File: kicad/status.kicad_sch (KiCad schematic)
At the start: 48 parts, among them J1 Bus_PCI_Express_x1, J2 PPTC041LGBN-RC, J3 Conn_01x04, J5 TF-115-BCP9, J6 USB_C_Receptacle_USB2.0_16P, J7 Conn_01x02, U1 MCP25625T-E/ML, U2 RP2040, U4 W25Q128JVP, X1 ABM8-272-T3, Y1 X322516MLB4SI

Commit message: Update PCB Layout and Change file Names to Status
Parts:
- removed J5: TF-115-BCP9, TF115BCP9, symbol TF-115-BCP9:TF-115-BCP9
- added J4: 503398-1892, 503398-1892:MOLEX_503398-1892, symbol MicroSD:503398-1892
- added R15: 10K, Resistor_SMD:R_0402_1005Metric, symbol Device:R
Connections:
- net +3.3V: now also J2.3, S11.C, J4.4 (VDD); no longer J2.2
- net CS_SD: now also J4.2 (CD/DAT3^2)
- net GND: now also J2.4, J4.6 (VSS), J4.9 (VSS__1), J4.P1 (SHIELD), J4.P2 (SHIELD__1), J4.P3 (SHIELD__2), J4.P4 (SHIELD__3), R15.2; no longer J2.1, S11.A
- net MISO: now also J4.7 (DAT0)
- net MOSI: now also J4.3 (CMD)
- net SCK: now also J4.5 (CLK)
- net SCL: now also J2.2; no longer J2.3
- net SDA: now also J2.1; no longer J2.4
- net RUN: now reaches U2.26 (RUN)
- net RUN: now also S11.A, R15.1; no longer S11.C
- removed net +BAT: J1.A16 (PERp0), J1.A17 (PERn0), J1.A18 (GND), J1.B16 (GND), J1.B17 (~{PRSNT2}), J1.B18 (GND)
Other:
- moved on the sheet: S11

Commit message: Pcb layout updated
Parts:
- removed J1: Bus_PCI_Express_x1, Connector_PCBEdge:BUS_PCIexpress_x1, symbol Connector:Bus_PCI_Express_x1
- removed U1: MCP25625T-E/ML, challenge_template:QFN28_6X6MC_MCH, symbol challenge symbols:MCP25625T-E_ML
- added J5: Bus_PCI_Express_x1, Connector_PCBEdge:BUS_PCIexpress_x1, symbol Connector:Bus_PCI_Express_x1
- added U3: MCP25625T-E/ML, QFN28_6X6MC_MCH, symbol challenge symbols:MCP25625T-E_ML
- D1: JLC Link https://jlcpcb.com/partdetail/177361-BL_HKC37A_AVTRB/C165978 -> https://jlcpcb.com/partdetail/EverlightElec-16_213_T3D_AP1Q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; LCSC Part # C165978 -> C74340
- J4: JLC Link (none) -> https://jlcpcb.com/parts/componentSearch?searchTxt=%2050339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; JLC link https://jlcpcb.com/parts/componentSearch?searchTxt=%2050339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 -> (none); LCSC Part # (none) -> C428492
- R10, R13, R15, R7, R8, R9: JLC Link https://jlcpcb.com/partdetail/Yageo-RC0402JR0710KL/C60489 -> https://jlcpcb.com/partdetail/YAGEO-RC0402FR0710KL/C60490; LCSC Part # C60489 -> C60490
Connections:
- net +3.3V: now also J5.A10 (+3.3V), J5.A11 (~{PERST}), J5.A9 (+3.3V), J5.B10 (3.3Vaux), J5.B11 (~{WAKE}), J5.B9 (JTAG1), U3.11 (VIO), U3.3 (VDD)
- net +5V: now also J5.A12 (GND), J5.A13 (REFCLK+), J5.A14 (REFCLK-), J5.B12 (RSVD), J5.B13 (GND), J5.B14 (PETp0), U3.19 (VDDA)
- net CANH: now also J5.A1 (~{PRSNT1}), U3.13 (CANH)
- net CANL: now also J5.A3 (+12V), U3.12 (CANL)
- net CS: now also U3.1 (*CS)
- net GND: now also J5.A4 (GND), J5.A5 (JTAG2), J5.A6 (JTAG3), J5.A7 (JTAG4), J5.B1 (+12V), J5.B2 (+12V), J5.B3 (+12V), J5.B4 (GND), J5.B5 (SMCLK), J5.B6 (SMDAT), J5.B7 (GND), U3.18 (VSS), U3.22 (GND), U3.29 (EPAD)
- net INT: now also U3.25 (*INT)
- net MISO: now also U3.28 (SO)
- net MOSI: now also U3.27 (SI)
- net OSC1: now also U3.21 (OSC1)
- net OSC2: now also U3.20 (OSC2)
- net RESET: now also U3.2 (*RESET)
- net RX: now also U3.10 (RXD), U3.5 (RXCAN)
- net SCK: now also U3.26 (SCK)
- net STBY: now also U3.15 (STBY)
- net TX: now also U3.16 (TXD), U3.4 (TXCAN)
- no-connect marks 17 -> 39

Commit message: SD Card Update
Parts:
- added R16, R17, R18, R19: 10K, Resistor_SMD:R_0402_1005Metric, symbol Device:R
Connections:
- net +3.3V: now also R16.1, R17.1, R18.1, R19.1
- net MISO: now also R17.2
- net MOSI: now also R16.2
- net at J4.1 (DAT2): now also R19.2
- net at J4.8 (DAT1): now also R18.2
- no-connect marks 39 -> 37

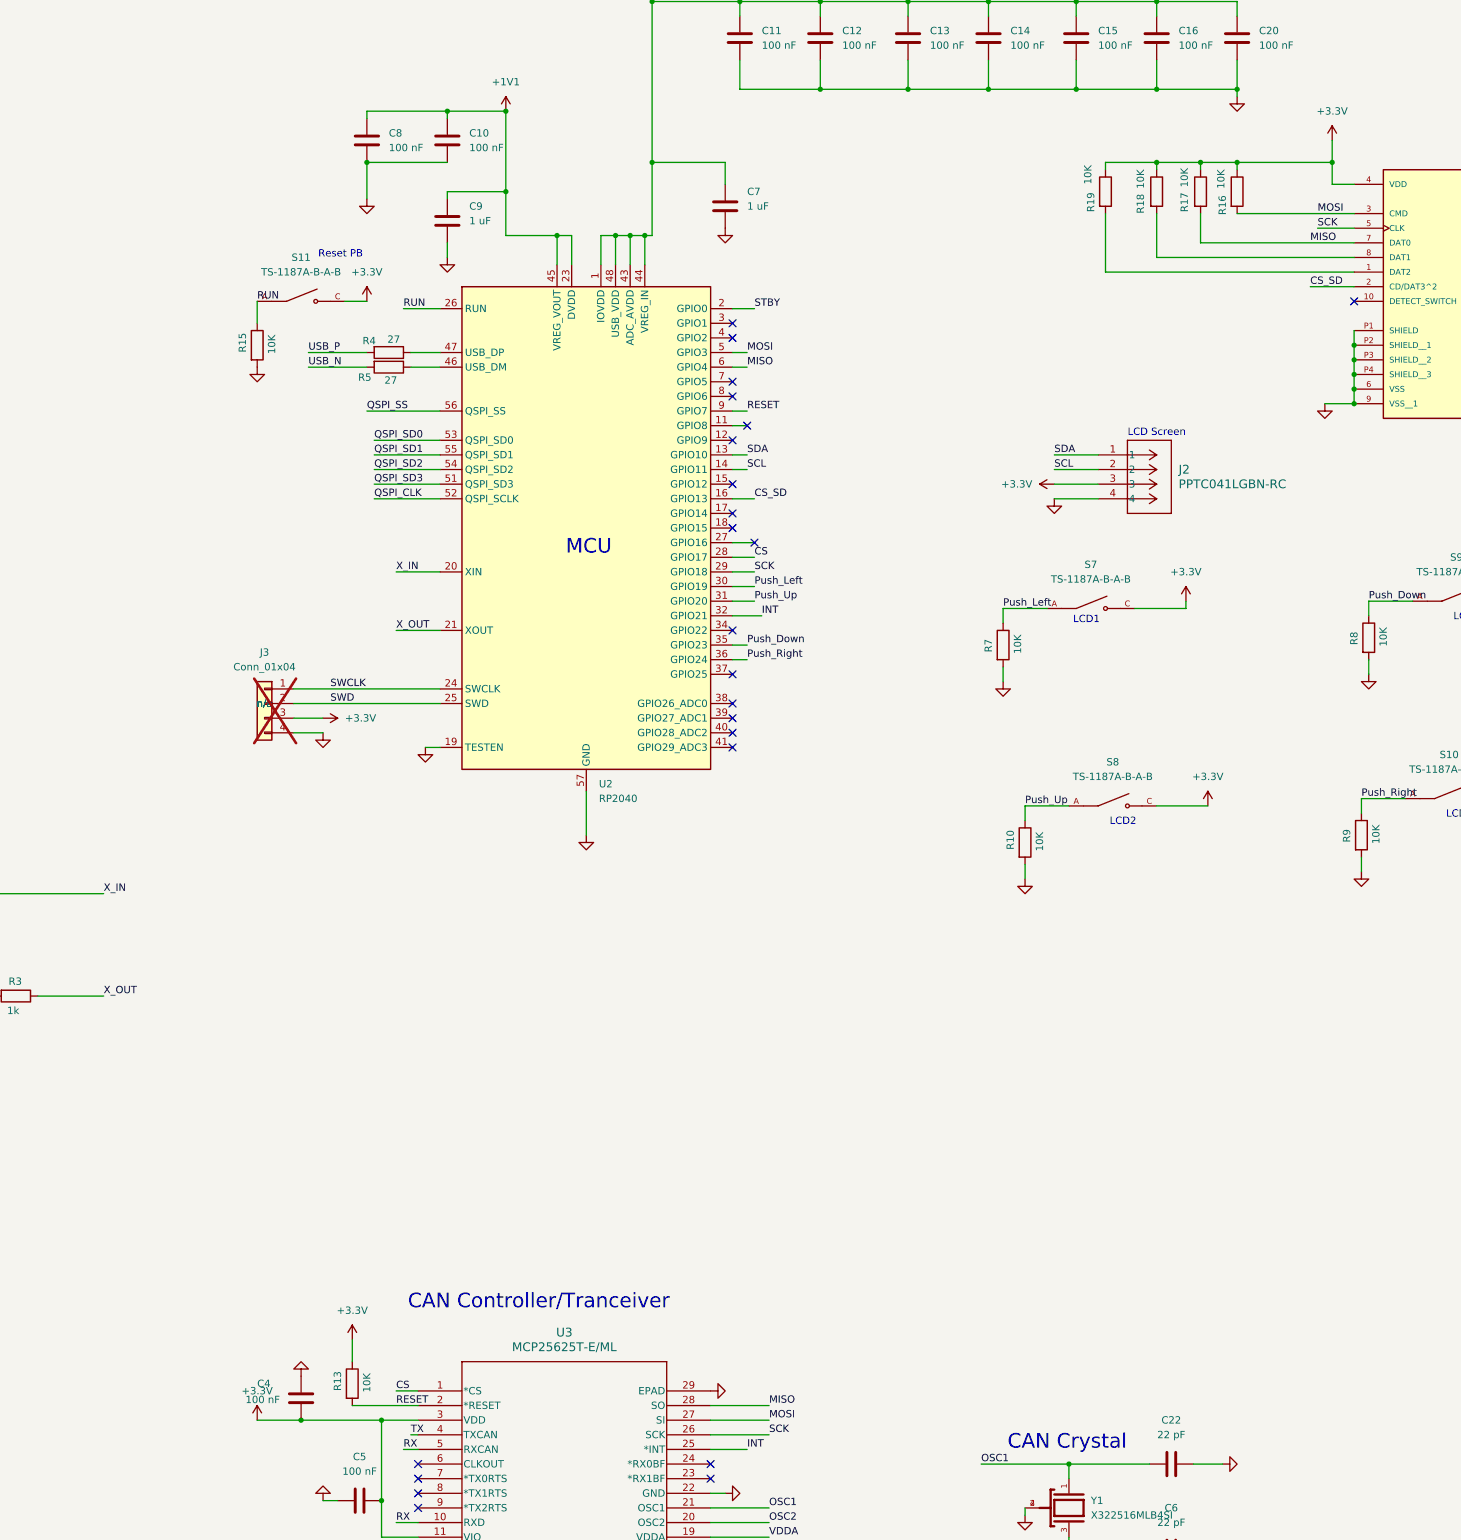
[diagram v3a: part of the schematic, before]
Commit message: General Updates
Moved CAN transmitter to separate SPI line.
Updated rp2040 clock.
Fixed debug pins.
Updated nets.
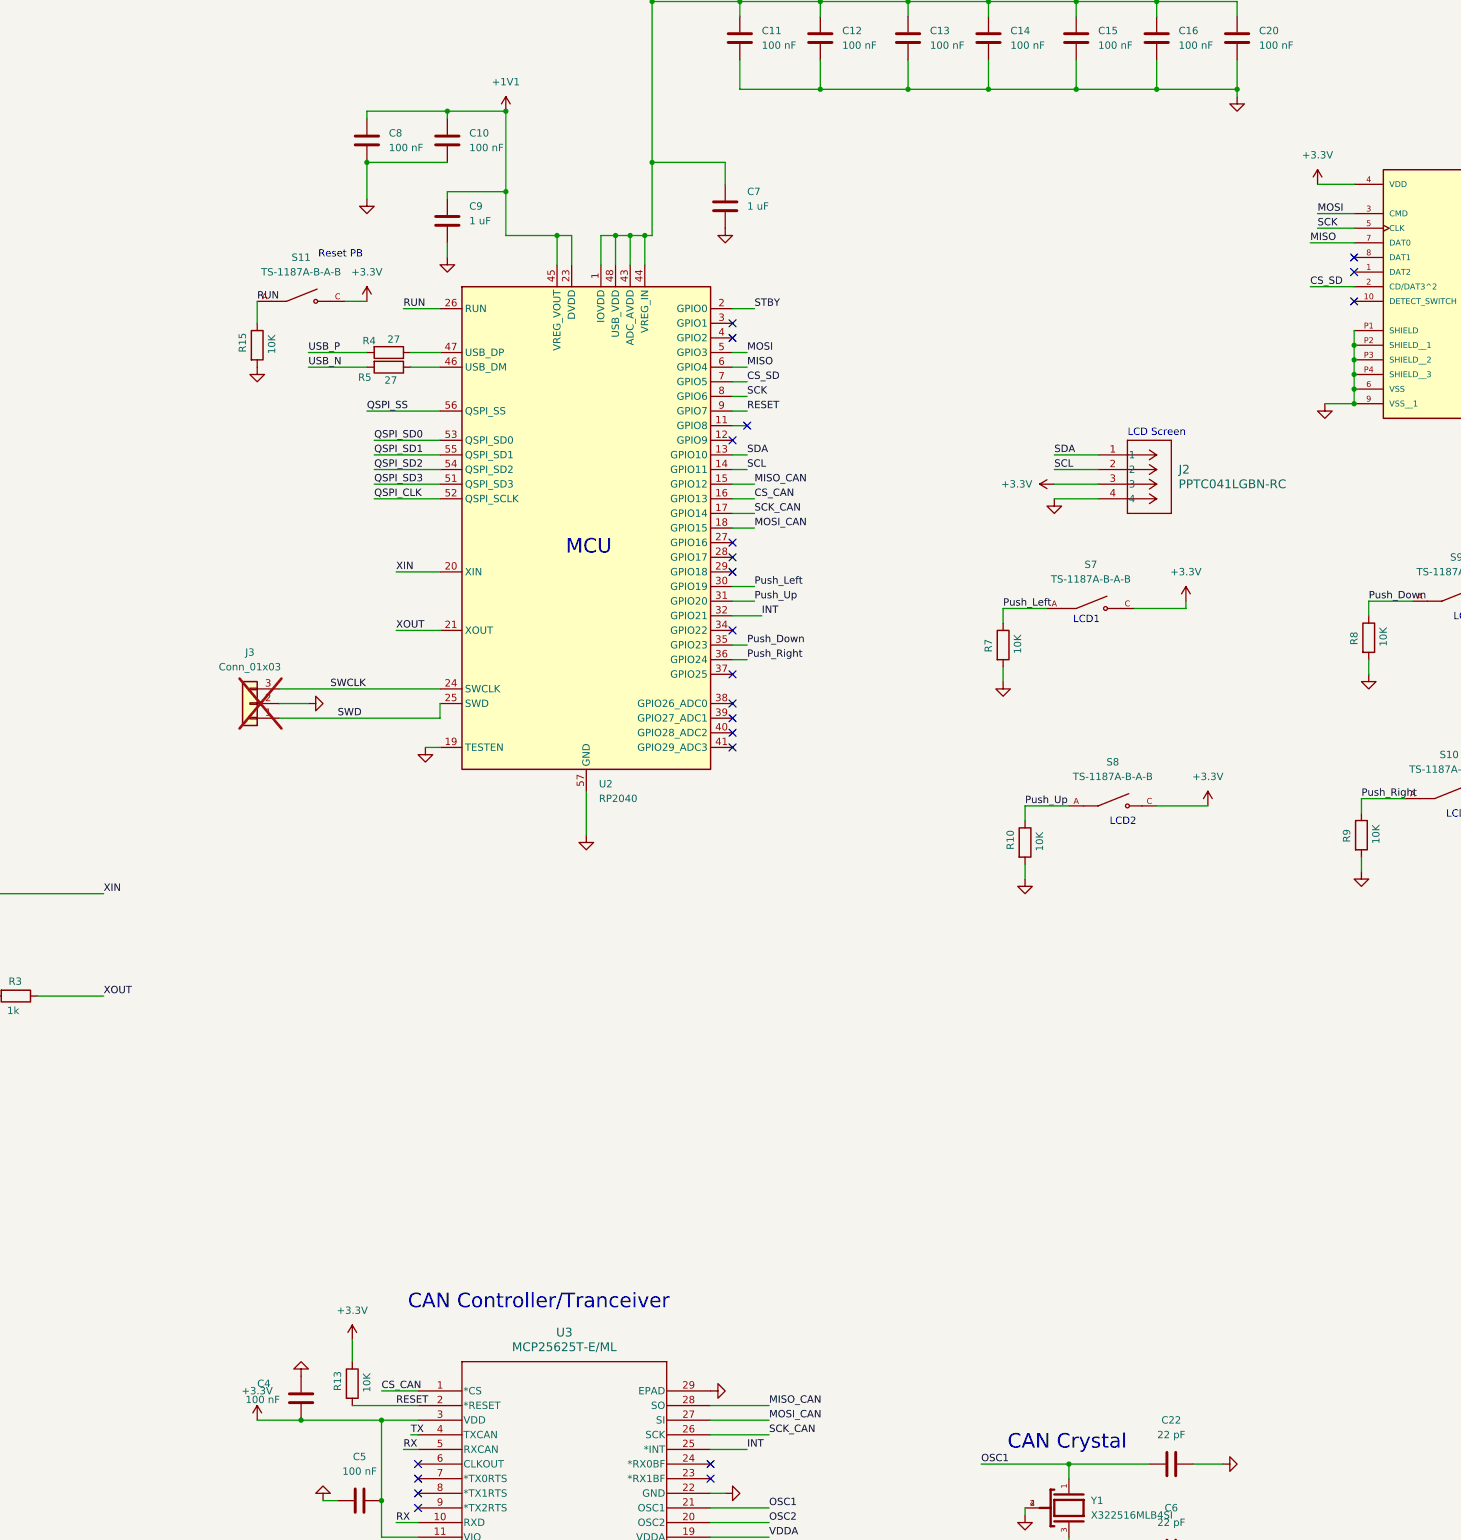
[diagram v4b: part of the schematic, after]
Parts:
- removed J3: Conn_01x04, Connector:NS-Tech_Grove_1x04_P2mm_Vertical, symbol Connector_Generic:Conn_01x04
- removed R16, R17, R18, R19: 10K, Resistor_SMD:R_0402_1005Metric, symbol Device:R
- added J3: Conn_01x03, symbol Connector_Generic:Conn_01x03
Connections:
- net CS_SD: now also U2.7 (GPIO5); no longer U2.16 (GPIO13)
- net GND: now also J3.2 (Pin_2)
- net MISO: no longer U3.28 (SO)
- net MOSI: no longer U3.27 (SI)
- net SCK: now also U2.8 (GPIO6); no longer U2.29 (GPIO18), U3.26 (SCK)
- net SWCLK: now also J3.3 (Pin_3)
- net SWD: now also J3.1 (Pin_1)
- net MISO_CAN: now reaches U2.15 (GPIO12)
- net MISO_CAN: now also U3.28 (SO)
- net SCK_CAN: now reaches U2.17 (GPIO14)
- net SCK_CAN: now also U3.26 (SCK)
- net MOSI_CAN: now reaches U2.18 (GPIO15)
- net MOSI_CAN: now also U3.27 (SI)
- net CS: no longer names the net of U2.28 (GPIO17)
- net CS: no longer U3.1 (*CS)
- net X_IN renamed XIN
- net X_OUT renamed XOUT
- new net CS_CAN: U2.16 (GPIO13), U3.1 (*CS)
- no-connect marks 37 -> 36

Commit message: General update schematic and PCB
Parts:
- added R16, R17, R18, R19: 10K, Resistor_SMD:R_0402_1005Metric, symbol Device:R
- J3: footprint (none) -> challenge_template:PinHeader_1x03_P2.54mm_Vertical
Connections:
- net +3.3V: now also R16.1, R17.1, R18.1, R19.1
- net MISO: now also R17.2
- net MOSI: now also R16.2
- net at J4.1 (DAT2): now also R19.2
- net at J4.8 (DAT1): now also R18.2
- no-connect marks 36 -> 34

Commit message: PCB Layout Update
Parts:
- removed J7: Conn_01x02, Connector_PinHeader_2.54mm:PinHeader_1x02_P2.54mm_Vertical, symbol Connector_Generic:Conn_01x02
- removed R15, R7, R8: 10K, Resistor_SMD:R_0402_1005Metric, symbol Device:R
- added R20, R21, R22: 10K, Resistor_SMD:R_0402_1005Metric, symbol Device:R
- added R24, R25, R26: 1k, Resistor_SMD:R_0402_1005Metric, symbol Device:R
- added S12: TS-1187A-B-A-B, Nicolas Library:SW_TS-1187A-B-A-B, symbol TS-1187A-B-A-B:TS-1187A-B-A-B
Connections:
- net +3.3V: now also R9.2, R24.2, R25.2, R26.2; no longer S10.C, S11.C, S7.C, S8.C, S9.C
- net GND: now also R10.1, S11.A, R20.1, R21.1, R22.1, S12.A; no longer R10.2, R9.2
- net Push_Down: now also R20.2
- net Push_Left: now also R22.2
- net Push_Right: now also R10.2; no longer R9.1
- net Push_Up: now also R21.2; no longer R10.1
- net RUN: now also S11.C; no longer S11.A
- net ~{USB_BOOT_S}: now also S12.C
- new net: R9.1, S10.C
- new net: R25.1, S8.C
- new net: R26.1, S9.C
- new net: R24.1, S7.C
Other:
- moved on the sheet: R9, S11

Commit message: PCB update
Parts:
- removed J2: PPTC041LGBN-RC, Nicolas Library:CONN_PPTC041LGBN-RC_SUL, symbol 2025-05-16_00-29-22:PPTC041LGBN-RC
- added U1: DM-OLED096-636, DM-OLED096-636:MODULE_DM-OLED096-636, symbol DM-OLED096-636:DM-OLED096-636
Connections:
- net +3.3V: now also U1.2 (VCC_IN)
- net GND: now also U1.1 (GND)
- net SCL: now also U1.3 (SCL)
- net SDA: now also U1.4 (SDA)
